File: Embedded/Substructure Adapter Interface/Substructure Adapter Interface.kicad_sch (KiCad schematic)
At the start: 3 parts, among them J1 Conn_01x02_Socket, J2 Conn_02x10_Odd_Even

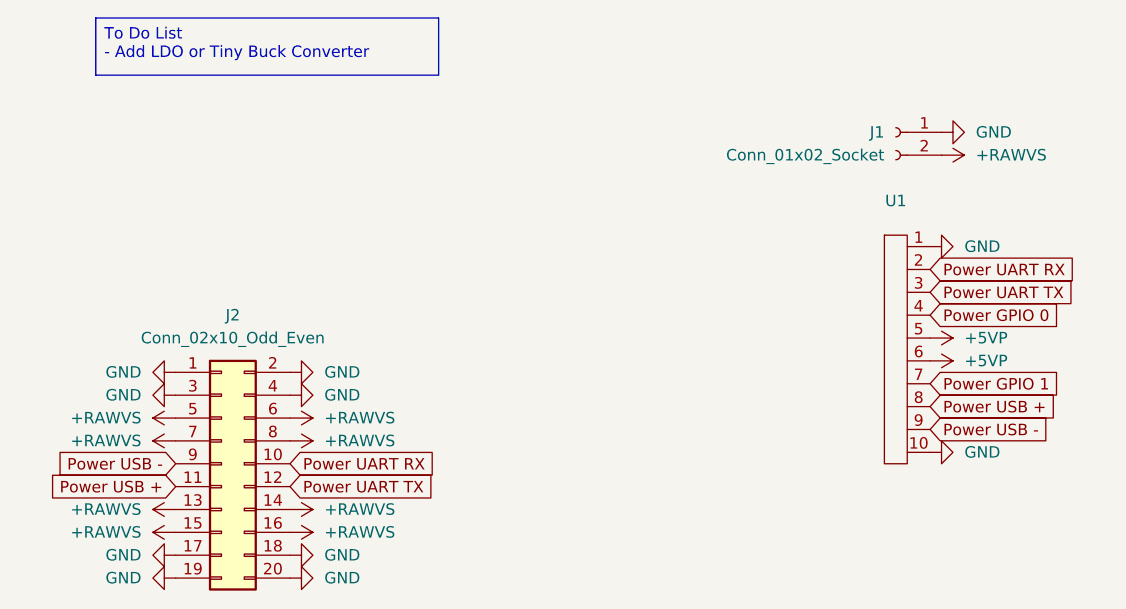
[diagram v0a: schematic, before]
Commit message: Added PCB Component Placement and Routing
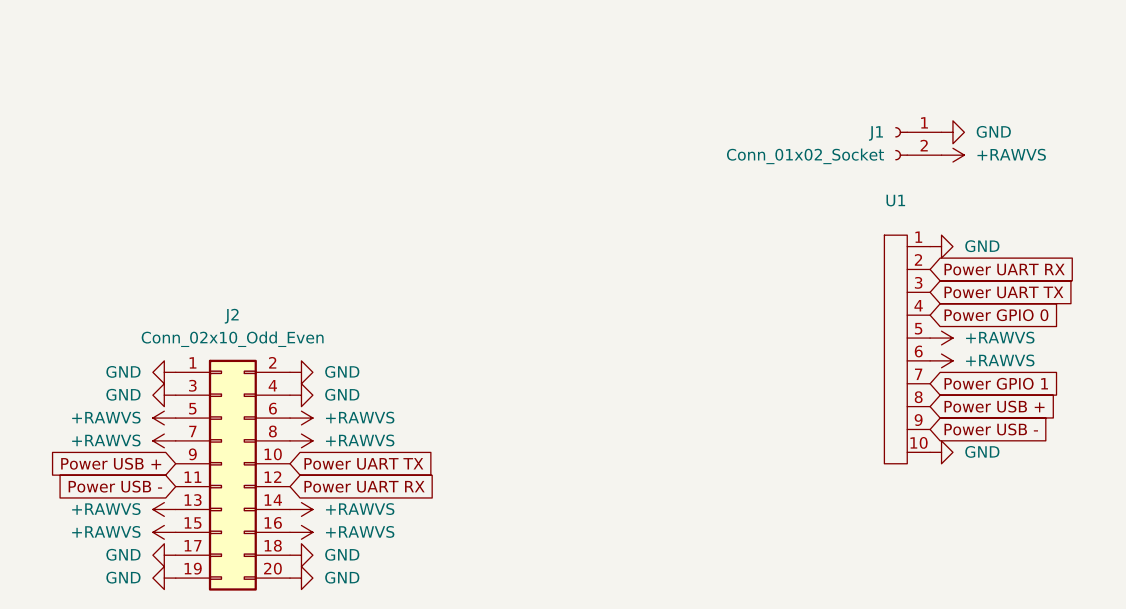
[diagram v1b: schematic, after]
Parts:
- U1: footprint (none) -> FFC:FFC 0.8mm 10P
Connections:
- net +5VP is gone; now on net +RAWVS: U1.5, U1.6
- net Power UART RX: now also J2.12 (Pin_12); no longer J2.10 (Pin_10)
- net Power UART TX: now also J2.10 (Pin_10); no longer J2.12 (Pin_12)
- net Power USB +: now also J2.9 (Pin_9); no longer J2.11 (Pin_11)
- net Power USB -: now also J2.11 (Pin_11); no longer J2.9 (Pin_9)

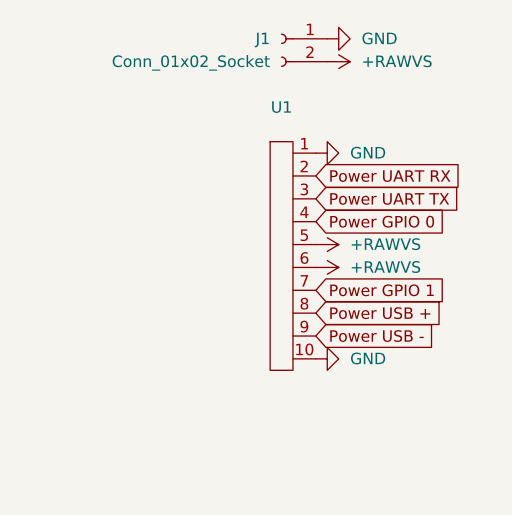
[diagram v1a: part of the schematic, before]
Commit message: Modified Ports to fit FFC orientations
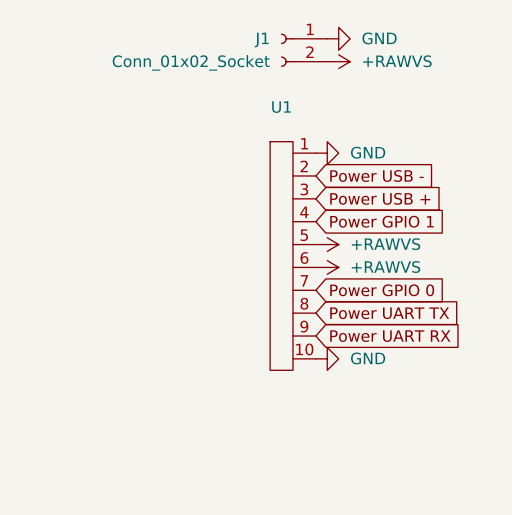
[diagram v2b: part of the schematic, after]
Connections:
- net Power GPIO 0: now also U1.7; no longer U1.4
- net Power GPIO 1: now also U1.4; no longer U1.7
- net Power UART RX: now also U1.9; no longer U1.2
- net Power UART TX: now also U1.8; no longer U1.3
- net Power USB +: now also U1.3; no longer U1.8
- net Power USB -: now also U1.2; no longer U1.9
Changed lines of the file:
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@@
 	(global_label "Power UART TX"
 		(shape input)
-		(at 118.11 55.88 0)
+		(at 118.11 68.58 0)
 		(fields_autoplaced yes)
 		(effects
@@
 		)
 		(property "Intersheetrefs" "${INTERSHEET_REFS}"
-			(at 135.4885 55.88 0)
+			(at 135.4885 68.58 0)
 			(effects
 				(font
@@
 	(global_label "Power UART RX"
 		(shape input)
-		(at 118.11 53.34 0)
+		(at 118.11 71.12 0)
 		(fields_autoplaced yes)
 		(effects
@@
 		)
 		(property "Intersheetrefs" "${INTERSHEET_REFS}"
-			(at 135.7909 53.34 0)
+			(at 135.7909 71.12 0)
 			(effects
 				(font
@@
 	(global_label "Power USB -"
 		(shape input)
-		(at 118.11 71.12 0)
+		(at 118.11 53.34 0)
 		(fields_autoplaced yes)
 		(effects
@@
 		)
 		(property "Intersheetrefs" "${INTERSHEET_REFS}"
-			(at 134.0371 71.12 0)
+			(at 134.0371 53.34 0)
 			(effects
 				(font
@@
 	(global_label "Power USB +"
 		(shape input)
-		(at 118.11 68.58 0)
+		(at 118.11 55.88 0)
 		(fields_autoplaced yes)
 		(effects
@@
 		)
 		(property "Intersheetrefs" "${INTERSHEET_REFS}"
-			(at 134.0371 68.58 0)
+			(at 134.0371 55.88 0)
 			(effects
 				(font
@@
 	(global_label "Power GPIO 1"
 		(shape input)
-		(at 118.11 66.04 0)
+		(at 118.11 58.42 0)
 		(fields_autoplaced yes)
 		(effects
@@
 		)
 		(property "Intersheetrefs" "${INTERSHEET_REFS}"
-			(at 134.3395 66.04 0)
+			(at 134.3395 58.42 0)
 			(effects
 				(font
@@
 	(global_label "Power GPIO 0"
 		(shape input)
-		(at 118.11 58.42 0)
+		(at 118.11 66.04 0)
 		(fields_autoplaced yes)
 		(effects
@@
 		)
 		(property "Intersheetrefs" "${INTERSHEET_REFS}"
-			(at 134.3395 58.42 0)
+			(at 134.3395 66.04 0)
 			(effects
 				(font
